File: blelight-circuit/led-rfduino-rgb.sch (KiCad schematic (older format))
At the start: 14 parts, among them P1 POWER_REGULATOR, Q1 N_CHAN_MOSFET, Q2 N_CHAN_MOSFET, Q3 N_CHAN_MOSFET

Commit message: fixed pcb
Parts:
- added PWR1: PWR_INPUT, symbol PWR_INPUT
- added USB1: USB-PROGRAMMER, symbol USB-PROGRAMMER
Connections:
- net at BLE1.13 (+3V), P1.2 (VOUT), VR1.1: now also USB1.2 (+3V)
- net at BLE1.14 (RESET): now also USB1.3 (RESET)
- net at BLE1.15 (FACTORY): now also USB1.4 (FACTORY)
- net at BLE1.16 (GPIO_0/AREF): now also USB1.5 (GPIO_0/AREF)
- net at BLE1.17 (GPIO_1): now also USB1.6 (GPIO_1)
- net +12V: no longer names the net of P1.1 (VIN), R4.2
- net +12V: now also PWR1.1 (VCC)
- net GND: no longer names the net of BLE1.12 (GND), P1.3 (GND), Q1.1 (S), Q2.1 (S), Q3.1 (S), R1.2, R2.2, R3.2, R5.2
- net GND: now also PWR1.2 (GND), USB1.1 (GND)
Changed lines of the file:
@@
 Sheet 1 1
 Title ""
-Date "22 feb 2015"
+Date "24 feb 2015"
 Rev ""
 Comp ""
@@
 Wire Wire Line
 	1800 700  1800 3300
-$Comp
-L +12V #PWR01
-U 1 1 54E928C0
-P 6300 3300
-F 0 "#PWR01" H 6300 3250 20  0001 C CNN
-F 1 "+12V" H 6300 3400 30  0000 C CNN
-F 2 "" H 6300 3300 60  0000 C CNN
-F 3 "" H 6300 3300 60  0000 C CNN
-	1    6300 3300
-	0    1    1    0
-$EndComp
-$Comp
-L GND #PWR02
-U 1 1 54E928CF
-P 6050 3400
-F 0 "#PWR02" H 6050 3400 30  0001 C CNN
-F 1 "GND" H 6050 3330 30  0001 C CNN
-F 2 "" H 6050 3400 60  0000 C CNN
-F 3 "" H 6050 3400 60  0000 C CNN
-	1    6050 3400
-	1    0    0    -1
-$EndComp
-Wire Wire Line
-	6050 3300 6050 3400
+Wire Wire Line
+	1800 3300 6050 3300
 Connection ~ 6050 3300
 Wire Wire Line
@@
 	6750 2500 6300 2500
 Wire Wire Line
-	6300 2000 6300 1400
-Wire Wire Line
-	1800 3300 6050 3300
+	6300 1400 6300 2000
 Connection ~ 5500 3300
 Connection ~ 4950 3300
@@
 Wire Wire Line
 	4300 1600 4000 1600
+$Comp
+L PWR_INPUT PWR1
+U 1 1 54ECB369
+P 6150 3700
+F 0 "PWR1" H 6150 3450 60  0000 C CNN
+F 1 "PWR_INPUT" H 6150 4050 60  0000 C CNN
+F 2 "" H 6150 3700 60  0000 C CNN
+F 3 "" H 6150 3700 60  0000 C CNN
+	1    6150 3700
+	0    1    1    0
+$EndComp
+$Comp
+L USB-PROGRAMMER USB1
+U 1 1 54ECB74F
+P 3150 2700
+F 0 "USB1" H 3200 2150 60  0000 C CNN
+F 1 "USB-PROGRAMMER" H 3150 3000 60  0000 C CNN
+F 2 "" H 3150 2700 60  0000 C CNN
+F 3 "" H 3150 2700 60  0000 C CNN
+	1    3150 2700
+	1    0    0    -1
+$EndComp
+Wire Wire Line
+	2750 2550 2450 2550
+Wire Wire Line
+	2450 2550 2450 3300
+Connection ~ 2450 3300
+Wire Wire Line
+	2750 2650 2750 2500
+Wire Wire Line
+	2750 2500 2200 2500
+Wire Wire Line
+	2200 2500 2200 1500
+Connection ~ 2200 1500
+Wire Wire Line
+	2450 1600 2300 1600
+Wire Wire Line
+	2300 1600 2300 2750
+Wire Wire Line
+	2300 2750 2750 2750
+Wire Wire Line
+	2750 2850 2350 2850
+Wire Wire Line
+	2350 2850 2350 1700
+Wire Wire Line
+	2350 1700 2450 1700
+Wire Wire Line
+	2550 2950 2750 2950
+Wire Wire Line
+	2550 1800 2550 2950
+Wire Wire Line
+	2550 1800 2450 1800
+Wire Wire Line
+	2750 3050 2650 3050
+Wire Wire Line
+	2650 3050 2650 2200
+Wire Wire Line
+	2650 2200 2400 2200
+Wire Wire Line
+	2400 2200 2400 1900
+Wire Wire Line
+	2400 1900 2450 1900
 $EndSCHEMATC

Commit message: lightserver working
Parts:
- added R6, R7: 39, 3W, ~, symbol R
- R1, R2, R3: value 10k -> 20k
- R4: value 3ohm 1W -> 13.9, 2W
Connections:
- net at D1.1 (A), D2.1 (A), D3.1 (A): now also P1.1 (VIN), PWR1.1 (VCC); no longer R4.1
- net at D3.2 (K): now also R7.1; no longer Q3.3 (D)
- net at D2.2 (K): now also R6.1; no longer Q2.3 (D)
- net at D1.2 (K): now also R4.1; no longer Q1.3 (D)
- new net: Q1.3 (D), R4.2
- new net: Q2.3 (D), R6.2
- new net: Q3.3 (D), R7.2
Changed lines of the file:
@@
 Sheet 1 1
 Title ""
-Date "24 feb 2015"
+Date "21 mar 2015"
 Rev ""
 Comp ""
@@
 Comment4 ""
 $EndDescr
-$Comp
-L R R4
-U 1 1 54E9181E
-P 6300 2250
-F 0 "R4" V 6380 2250 40  0000 C CNN
-F 1 "3ohm 1W" V 6307 2251 40  0000 C CNN
-F 2 "~" V 6230 2250 30  0000 C CNN
-F 3 "~" H 6300 2250 30  0000 C CNN
-	1    6300 2250
-	1    0    0    -1
-$EndComp
 $Comp
 L RFDUINO BLE1
@@
 P 4400 3050
 F 0 "R1" V 4480 3050 40  0000 C CNN
-F 1 "10k" V 4407 3051 40  0000 C CNN
+F 1 "20k" V 4407 3051 40  0000 C CNN
 F 2 "~" V 4330 3050 30  0000 C CNN
 F 3 "~" H 4400 3050 30  0000 C CNN
@@
 P 4950 3050
 F 0 "R2" V 5030 3050 40  0000 C CNN
-F 1 "10k" V 4957 3051 40  0000 C CNN
+F 1 "20k" V 4957 3051 40  0000 C CNN
 F 2 "~" V 4880 3050 30  0000 C CNN
 F 3 "~" H 4950 3050 30  0000 C CNN
@@
 P 5500 3050
 F 0 "R3" V 5580 3050 40  0000 C CNN
-F 1 "10k" V 5507 3051 40  0000 C CNN
+F 1 "20k" V 5507 3051 40  0000 C CNN
 F 2 "~" V 5430 3050 30  0000 C CNN
 F 3 "~" H 5500 3050 30  0000 C CNN
@@
 $EndComp
 Wire Wire Line
-	1800 700  1800 3300
-Wire Wire Line
-	1800 3300 6050 3300
+	1800 700  1800 1400
+Wire Wire Line
+	1800 1400 1800 3300
+Wire Wire Line
+	1800 3300 2250 3300
+Wire Wire Line
+	2250 3300 2450 3300
+Wire Wire Line
+	2450 3300 4400 3300
+Wire Wire Line
+	4400 3300 4700 3300
+Wire Wire Line
+	4700 3300 4950 3300
+Wire Wire Line
+	4950 3300 5250 3300
+Wire Wire Line
+	5250 3300 5500 3300
+Wire Wire Line
+	5500 3300 5800 3300
+Wire Wire Line
+	5800 3300 6050 3300
 Connection ~ 6050 3300
 Wire Wire Line
-	6300 3300 6300 2500
+	6300 1400 6300 1600
+Wire Wire Line
+	6300 1600 6300 1800
+Wire Wire Line
+	6300 1800 6300 2500
+Wire Wire Line
+	6300 2500 6300 3300
 $Comp
 L LED D3
@@
 Connection ~ 6300 1800
 Wire Wire Line
-	4700 1800 4700 2600
-Wire Wire Line
-	5250 1600 5250 2600
-Wire Wire Line
-	5800 1400 5800 2600
-Wire Wire Line
 	5800 3000 5800 3300
 Connection ~ 5800 3300
@@
 Connection ~ 1800 1400
 Wire Wire Line
-	2000 1500 2450 1500
+	2000 1500 2200 1500
+Wire Wire Line
+	2200 1500 2450 1500
 Connection ~ 2000 1500
 Wire Wire Line
 	2250 2600 2000 2600
 Wire Wire Line
-	2000 2000 2000 2100
+	2000 2000 2000 2050
+Wire Wire Line
+	2000 2050 2000 2100
 Wire Wire Line
 	2000 1500 2250 850
@@
 Wire Wire Line
 	6750 2500 6300 2500
-Wire Wire Line
-	6300 1400 6300 2000
 Connection ~ 5500 3300
 Connection ~ 4950 3300
@@
 Wire Wire Line
 	2400 1900 2450 1900
+Connection ~ 6300 2500
+$Comp
+L R R7
+U 1 1 550CBB60
+P 5800 2200
+F 0 "R7" V 5880 2200 40  0000 C CNN
+F 1 "39, 3W" V 5807 2201 40  0000 C CNN
+F 2 "~" V 5730 2200 30  0000 C CNN
+F 3 "~" H 5800 2200 30  0000 C CNN
+	1    5800 2200
+	1    0    0    -1
+$EndComp
+Wire Wire Line
+	5800 2600 5800 2450
+Wire Wire Line
+	5800 1950 5800 1400
+$Comp
+L R R6
+U 1 1 550CBC4B
+P 5250 2200
+F 0 "R6" V 5330 2200 40  0000 C CNN
+F 1 "39, 3W" V 5257 2201 40  0000 C CNN
+F 2 "~" V 5180 2200 30  0000 C CNN
+F 3 "~" H 5250 2200 30  0000 C CNN
+	1    5250 2200
+	1    0    0    -1
+$EndComp
+Wire Wire Line
+	5250 2600 5250 2450
+Wire Wire Line
+	5250 1950 5250 1600
+$Comp
+L R R4
+U 1 1 550CBCFB
+P 4700 2150
+F 0 "R4" V 4780 2150 40  0000 C CNN
+F 1 "13.9, 2W" V 4707 2151 40  0000 C CNN
+F 2 "~" V 4630 2150 30  0000 C CNN
+F 3 "~" H 4700 2150 30  0000 C CNN
+	1    4700 2150
+	1    0    0    -1
+$EndComp
+Wire Wire Line
+	4700 1800 4700 1900
+Wire Wire Line
+	4700 2400 4700 2600
 $EndSCHEMATC

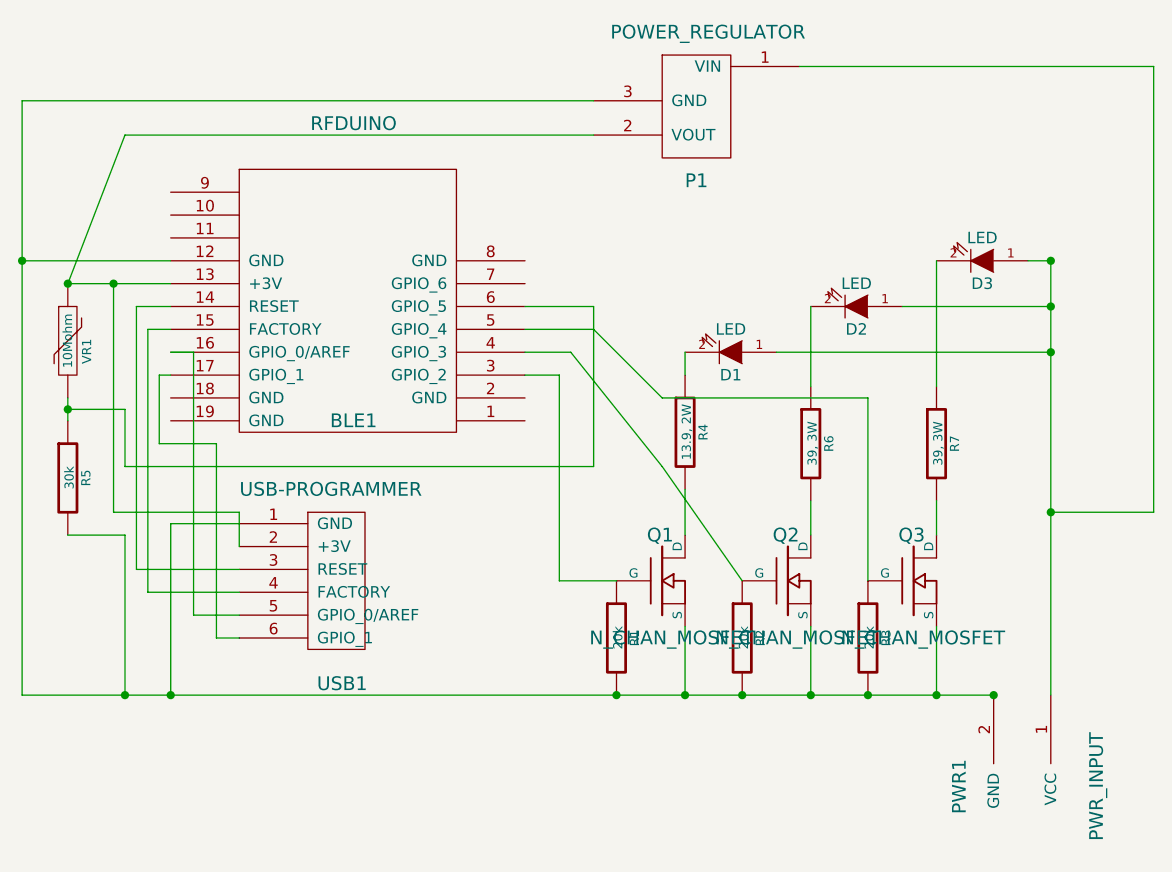
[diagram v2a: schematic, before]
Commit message: removed corners
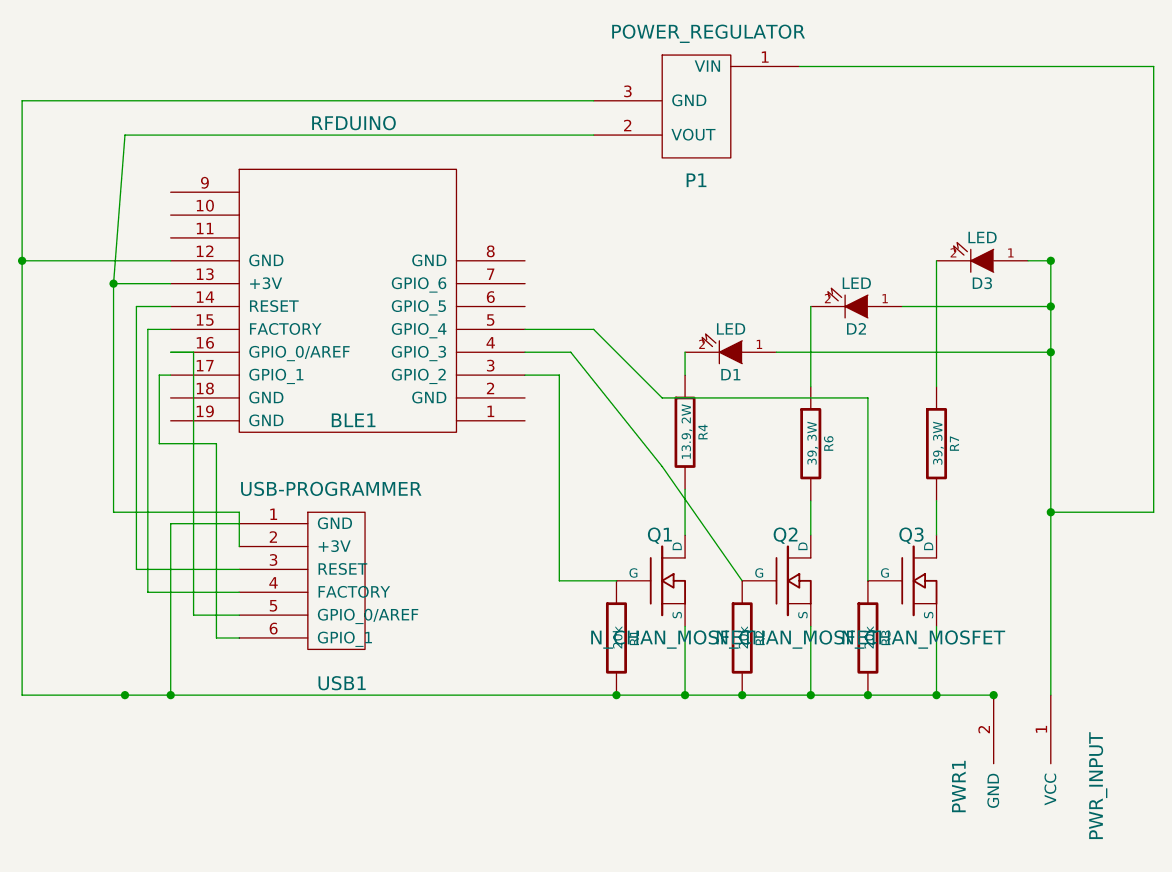
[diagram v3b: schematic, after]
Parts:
- removed R5: 30k, ~, symbol R
- removed VR1: 10Mohm, ~, symbol VR
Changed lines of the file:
@@
 Sheet 1 1
 Title ""
-Date "21 mar 2015"
+Date "27 mar 2015"
 Rev ""
 Comp ""
@@
 $EndComp
 Wire Wire Line
-	1800 700  1800 1400
-Wire Wire Line
-	1800 1400 1800 3300
-Wire Wire Line
-	1800 3300 2250 3300
-Wire Wire Line
-	2250 3300 2450 3300
-Wire Wire Line
-	2450 3300 4400 3300
-Wire Wire Line
-	4400 3300 4700 3300
-Wire Wire Line
-	4700 3300 4950 3300
-Wire Wire Line
-	4950 3300 5250 3300
-Wire Wire Line
-	5250 3300 5500 3300
-Wire Wire Line
-	5500 3300 5800 3300
-Wire Wire Line
-	5800 3300 6050 3300
+	1800 700  1800 3300
+Wire Wire Line
+	1800 3300 6050 3300
 Connection ~ 6050 3300
 Wire Wire Line
-	6300 1400 6300 1600
-Wire Wire Line
-	6300 1600 6300 1800
-Wire Wire Line
-	6300 1800 6300 2500
-Wire Wire Line
-	6300 2500 6300 3300
+	6300 1400 6300 3300
 $Comp
 L LED D3
@@
 Wire Wire Line
 	4300 700  1800 700
-$Comp
-L R R5
-U 1 1 54E92F15
-P 2000 2350
-F 0 "R5" V 2080 2350 40  0000 C CNN
-F 1 "30k" V 2007 2351 40  0000 C CNN
-F 2 "~" V 1930 2350 30  0000 C CNN
-F 3 "~" H 2000 2350 30  0000 C CNN
-	1    2000 2350
-	1    0    0    -1
-$EndComp
-Wire Wire Line
-	2250 2600 2250 3300
 Connection ~ 2250 3300
 Wire Wire Line
@@
 Connection ~ 1800 1400
 Wire Wire Line
-	2000 1500 2200 1500
-Wire Wire Line
 	2200 1500 2450 1500
-Connection ~ 2000 1500
-Wire Wire Line
-	2250 2600 2000 2600
-Wire Wire Line
-	2000 2000 2000 2050
-Wire Wire Line
-	2000 2050 2000 2100
-Wire Wire Line
-	2000 1500 2250 850
-$Comp
-L VR VR1
-U 1 1 54E943F3
-P 2000 1750
-F 0 "VR1" V 2060 1704 40  0000 C TNN
-F 1 "10Mohm" V 2000 1750 40  0000 C CNN
-F 2 "~" H 2000 1750 60  0000 C CNN
-F 3 "~" H 2000 1750 60  0000 C CNN
-	1    2000 1750
-	1    0    0    -1
-$EndComp
-Wire Wire Line
-	2250 2050 2000 2050
-Connection ~ 2000 2050
+Connection ~ 2200 1500
+Wire Wire Line
+	2200 1500 2250 850
 Wire Wire Line
 	4150 2800 4150 1900
@@
 Connection ~ 4950 3300
 Connection ~ 4400 3300
-Wire Wire Line
-	2250 2050 2250 2300
-Wire Wire Line
-	2250 2300 4300 2300
-Wire Wire Line
-	4300 2300 4300 1600
-Wire Wire Line
-	4300 1600 4000 1600
 $Comp
 L PWR_INPUT PWR1
@@
 Wire Wire Line
 	2200 2500 2200 1500
-Connection ~ 2200 1500
 Wire Wire Line
 	2450 1600 2300 1600
